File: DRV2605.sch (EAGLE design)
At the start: 107 parts, among them J1 BM06B-SRSS-TB, J2 BM06B-SRSS-TB, J3 BM06B-SRSS-TB, J4 BM06B-SRSS-TB, J5 BM06B-SRSS-TB, J6 JST_6_PIN_VERTICAL, U1 DRV2605L, U11 NRF51X22_QFQF, U2 DRV2605L, U3 DRV2605L, U4 DRV2605L, U5 DRV2605L, U6 DRV2605L, U7 BNO080, U8 TCA9548APWR, U9 TCA9548APWR, X1 32.768kHz, X2 8MHz, X4 16MHz, X5 32.768kHz, Y1 32.768kHz

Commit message: 6DRVs ARM IMU on board - done; palmIMU/battery/programming connector
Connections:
- removed net PS0/WAKE: U7.PS0/WAKE
- removed net PS1: U7.PS1
- removed net SCL/SCK/RX: R28.1, U7.H_SCL/SCLK/RX
- removed net SDA/MISO/TX: R29.1, U7.H_SDA/MISO/TX
- net EN6: now also U$9.PB14/I2S2_XD
- net GND: now also U7.PS0/WAKE, U7.PS1
- net IMU_SCL6: now also R28.1, U7.H_SCL/SCLK/RX
- net IMU_SDA6: now also R29.1, U7.H_SDA/MISO/TX
- net IN/TRIG6: now also U$9.PB15/I2S2_SD
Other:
- note added: "ARM Chip Circuit"
- note added: "BNO080"
- note added: "DRV2605"
- moved on the sheet: C1, C10, C11, C12, C2, C3, C4, C5, C6, C7, C8, C9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

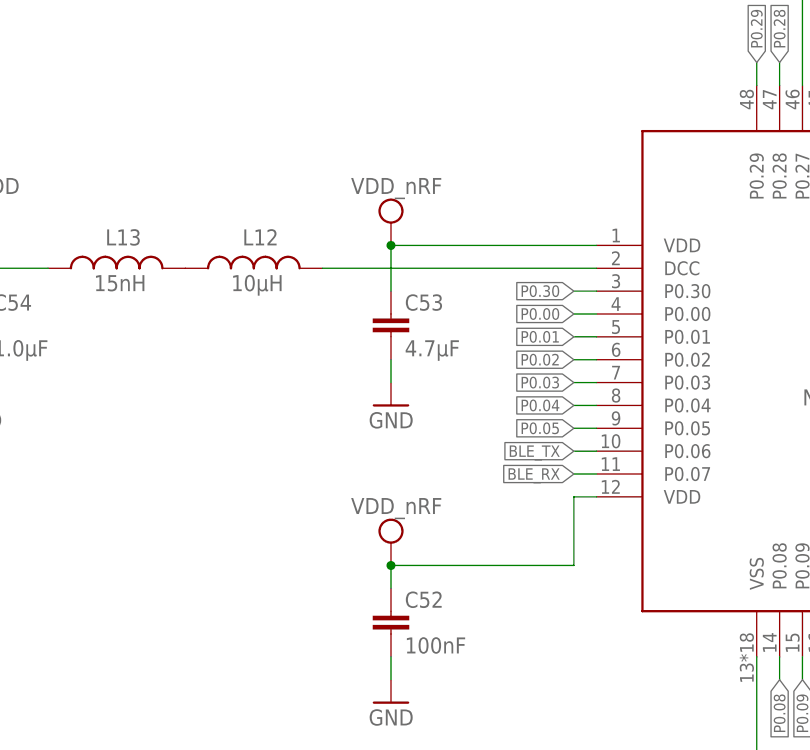
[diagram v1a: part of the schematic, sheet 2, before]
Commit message: glove connector;programming pins;NRF antenna left
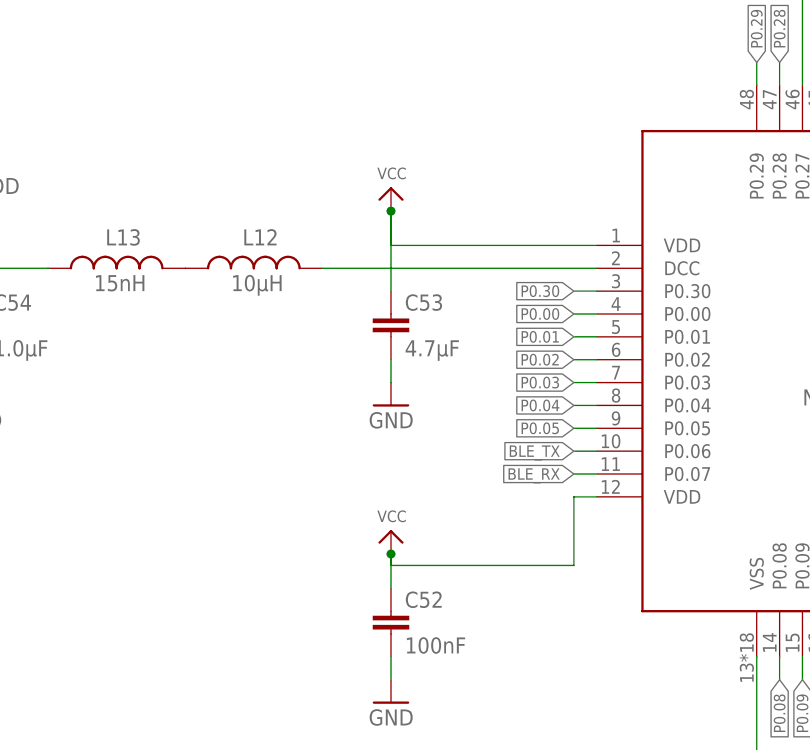
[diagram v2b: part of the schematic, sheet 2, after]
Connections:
- removed net 3.3V: C13.1, C32.1, R13.2, R14.2, R24.2, R26.2, R27.2, R28.2, R29.2, U7.VDD, U7.VDDIO
- removed net VDD_NRF: C52.1, C53.1, U11.VDD@01, U11.VDD@12
- net VCC: now also C13.1, C32.1, C52.1, C53.1, R13.2, R14.2, R24.2, R26.2, R27.2, R28.2, R29.2, U11.VDD@01, U11.VDD@12, U7.VDD, U7.VDDIO

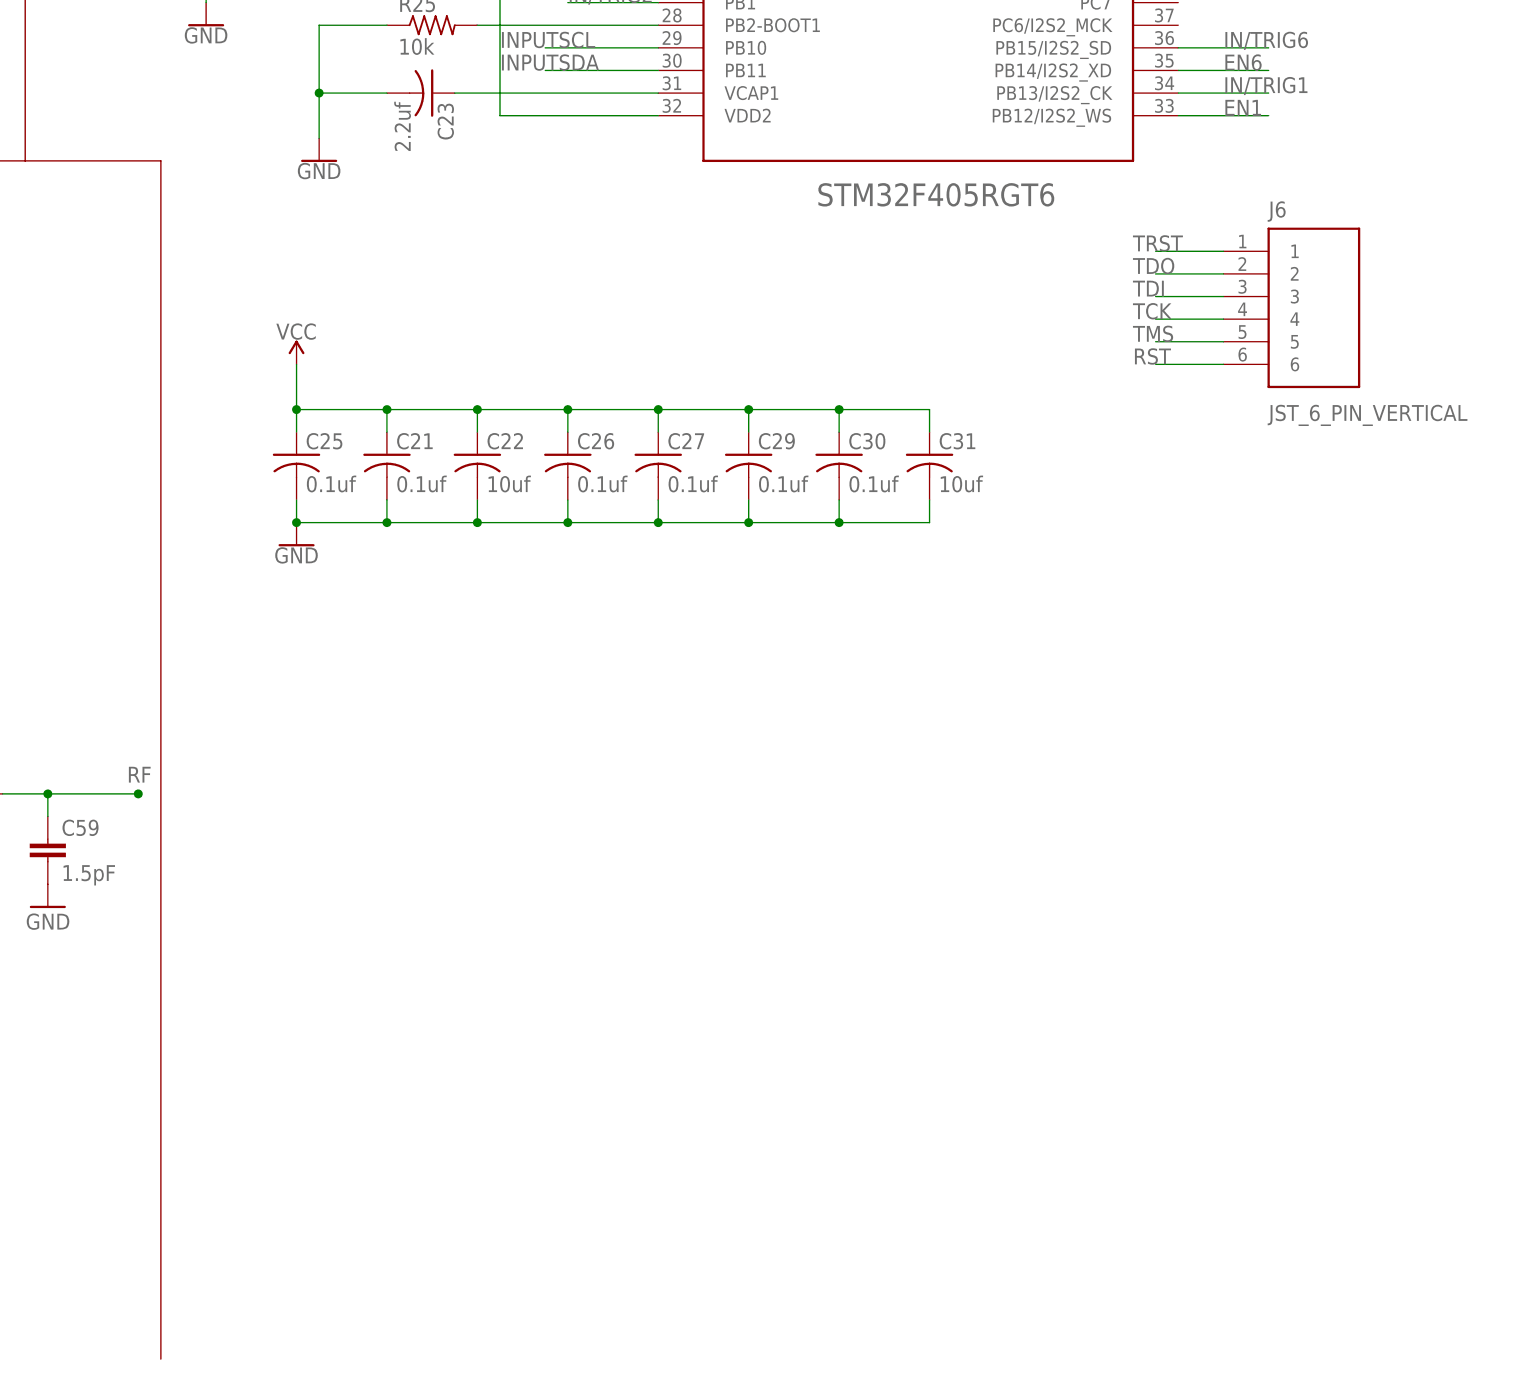
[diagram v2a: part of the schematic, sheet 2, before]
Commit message: glove connector;programming pins;NRF antenna
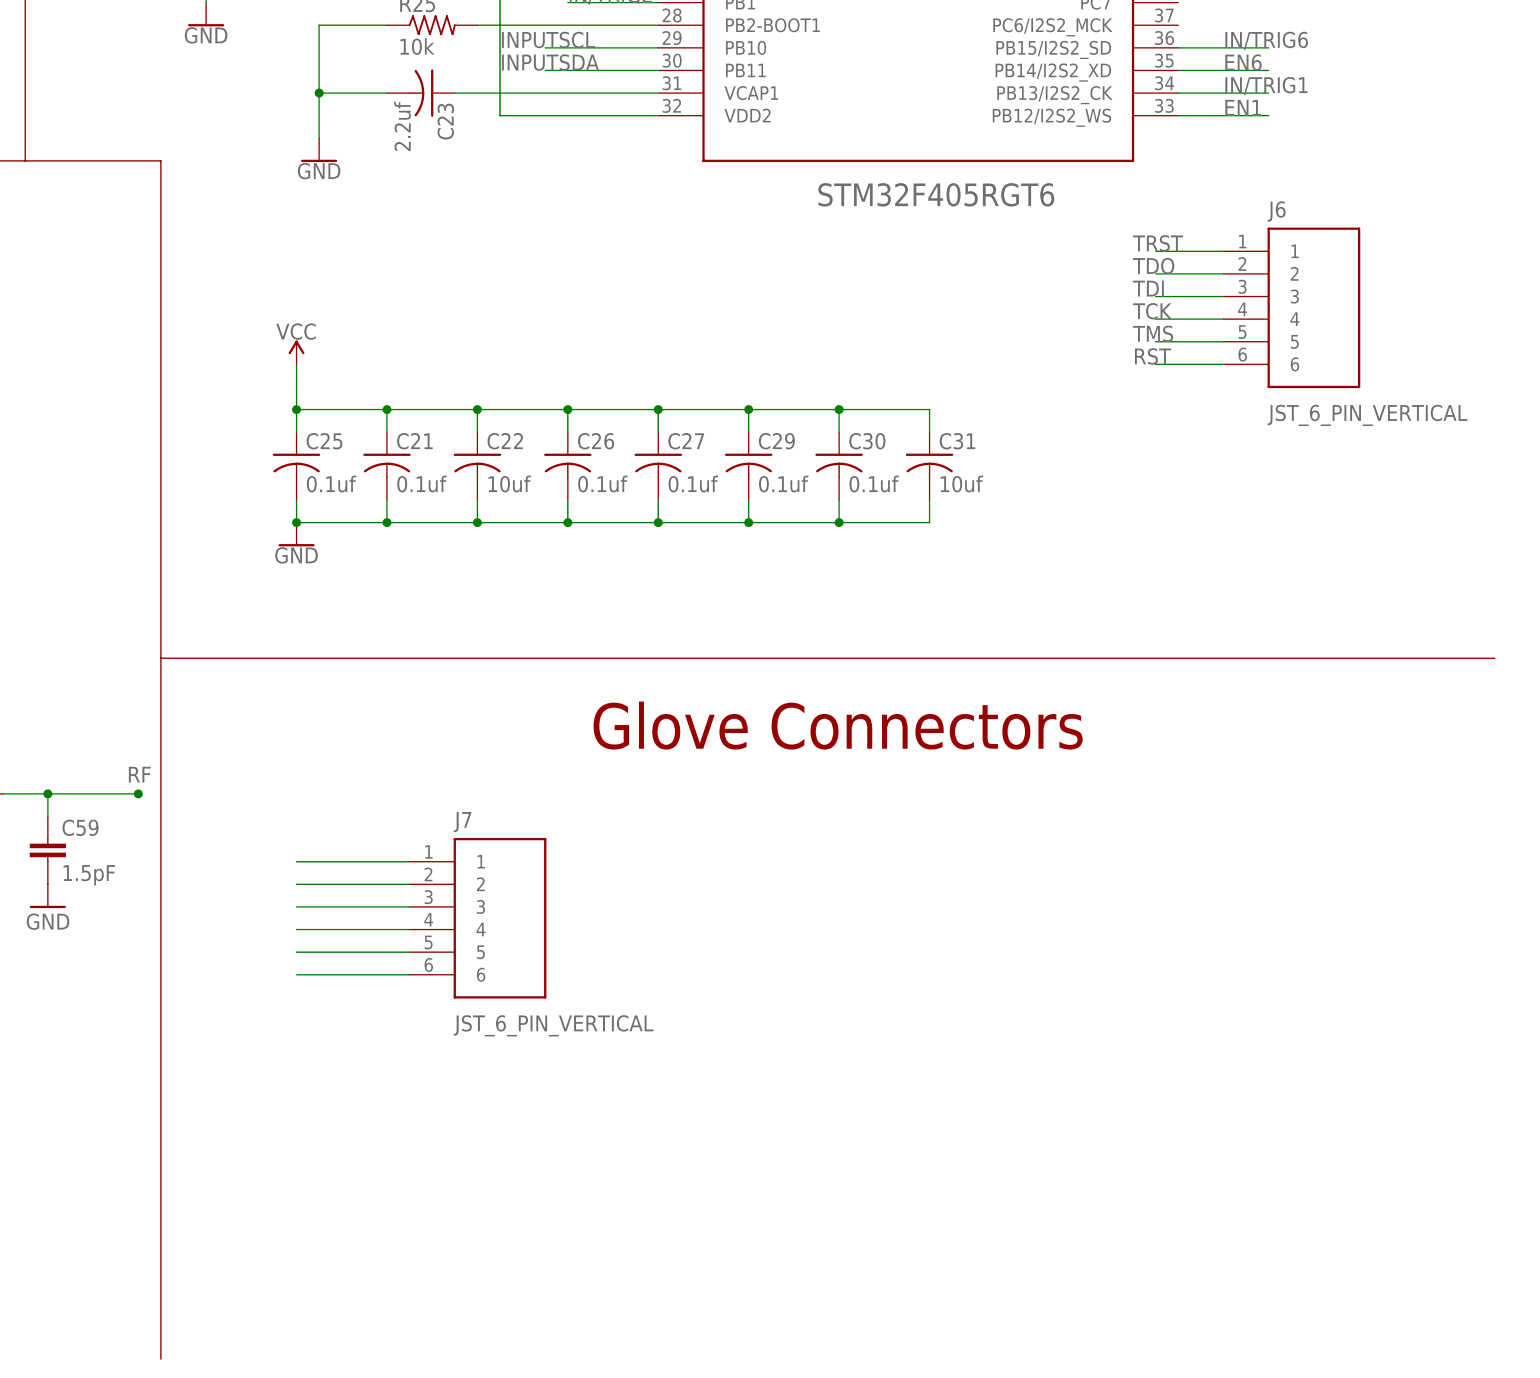
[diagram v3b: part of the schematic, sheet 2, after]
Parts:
- J7: value (none) -> JST_6_PIN_VERTICAL; device SparkFun-Connectors:CONN_04SMD2 -> SparkFun-Connectors:JST_6_PIN_VERTICAL
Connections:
- new net N$15: J7.1
- new net N$17: J7.2
- new net N$18: J7.3
- new net N$20: J7.4
- new net N$21: J7.5
- new net N$22: J7.6
- net +OUT6: no longer J7.3
- net -OUT6: no longer J7.4
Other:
- note added: "Glove Connectors"
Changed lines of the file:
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@@
 <part name="J4" library="SparkFun-Connectors" deviceset="JST_6_PIN_HORIZONTAL" device="" value="BM06B-SRSS-TB"/>
 <part name="J5" library="SparkFun-Connectors" deviceset="JST_6_PIN_HORIZONTAL" device="" value="BM06B-SRSS-TB"/>
-<part name="J7" library="SparkFun-Connectors" library_urn="urn:adsk.eagle:library:513" deviceset="CONN_04" device="SMD2" package3d_urn="urn:adsk.eagle:package:38096/1"/>
 <part name="U8" library="microbuilder" deviceset="TCA9548A" device="" value=" TCA9548APWR"/>
 <part name="R15" library="rcl" library_urn="urn:adsk.eagle:library:334" deviceset="R-US_" device="R0402" package3d_urn="urn:adsk.eagle:package:23547/2" value="10K"/>
@@
 <part name="P+11" library="microbuilder" deviceset="VCC" device=""/>
 <part name="P+12" library="microbuilder" deviceset="VCC" device=""/>
+<part name="J7" library="SparkFun-Connectors" library_urn="urn:adsk.eagle:library:513" deviceset="JST_6_PIN_VERTICAL" device="" package3d_urn="urn:adsk.eagle:package:38270/1"/>
 </parts>
 <sheets>
@@
 <instance part="J4" gate="A" x="142.24" y="30.48" rot="R180"/>
 <instance part="J5" gate="A" x="331.47" y="220.98" rot="R180"/>
-<instance part="J7" gate="G$1" x="331.47" y="157.48" rot="R180"/>
 <instance part="SUPPLY19" gate="G$1" x="317.5" y="64.77"/>
 <instance part="GND13" gate="1" x="317.5" y="49.53"/>
@@
 <label x="284.48" y="157.48" size="1.778" layer="95"/>
 </segment>
-<segment>
-<pinref part="J7" gate="G$1" pin="4"/>
-<wire x1="326.39" y1="152.4" x2="318.77" y2="152.4" width="0.1524" layer="91"/>
-<wire x1="318.77" y1="152.4" x2="317.5" y2="152.4" width="0.1524" layer="91"/>
-<label x="316.23" y="152.4" size="1.778" layer="95"/>
-</segment>
 </net>
 <net name="+OUT6" class="0">
@@
 <wire x1="279.4" y1="152.4" x2="287.02" y2="152.4" width="0.1524" layer="91"/>
 <label x="284.48" y="152.4" size="1.778" layer="95"/>
-</segment>
-<segment>
-<pinref part="J7" gate="G$1" pin="3"/>
-<wire x1="326.39" y1="154.94" x2="317.5" y2="154.94" width="0.1524" layer="91"/>
-<label x="317.5" y="154.94" size="1.778" layer="95"/>
 </segment>
 </net>
@@
 <wire x1="218.44" y1="137.16" x2="218.44" y2="256.54" width="0.1524" layer="94"/>
 <wire x1="218.44" y1="137.16" x2="233.68" y2="137.16" width="0.1524" layer="94"/>
-<wire x1="233.68" y1="137.16" x2="233.68" y2="2.54" width="0.1524" layer="94"/>
+<wire x1="233.68" y1="137.16" x2="233.68" y2="81.28" width="0.1524" layer="94"/>
 <text x="78.74" y="243.84" size="5.08" layer="94">TCA Chip Circuit</text>
+<wire x1="233.68" y1="81.28" x2="233.68" y2="2.54" width="0.1524" layer="94"/>
 <wire x1="45.72" y1="134.62" x2="45.72" y2="96.52" width="0.254" layer="97"/>
 <wire x1="45.72" y1="96.52" x2="91.44" y2="96.52" width="0.254" layer="97"/>
@@
 <text x="360.68" y="251.46" size="1.778" layer="94">Boot from flash</text>
 <text x="287.02" y="246.38" size="5.08" layer="94">ARM Chip Circuit</text>
+<wire x1="233.68" y1="81.28" x2="383.54" y2="81.28" width="0.1524" layer="94"/>
+<text x="281.94" y="71.12" size="5.08" layer="94">Glove Connectors</text>
 </plain>
 <instances>
@@
 <instance part="P+11" gate="VCC" x="55.88" y="74.93"/>
 <instance part="P+12" gate="VCC" x="55.88" y="36.83"/>
+<instance part="J7" gate="G$1" x="274.32" y="53.34"/>
 </instances>
 <busses>
@@
 </segment>
 </net>
+<net name="N$15" class="0">
+<segment>
+<pinref part="J7" gate="G$1" pin="1"/>
+<wire x1="261.62" y1="58.42" x2="248.92" y2="58.42" width="0.1524" layer="91"/>
+</segment>
+</net>
+<net name="N$17" class="0">
+<segment>
+<pinref part="J7" gate="G$1" pin="2"/>
+<wire x1="261.62" y1="55.88" x2="248.92" y2="55.88" width="0.1524" layer="91"/>
+</segment>
+</net>
+<net name="N$18" class="0">
+<segment>
+<pinref part="J7" gate="G$1" pin="3"/>
+<wire x1="261.62" y1="53.34" x2="248.92" y2="53.34" width="0.1524" layer="91"/>
+</segment>
+</net>
+<net name="N$20" class="0">
+<segment>
+<pinref part="J7" gate="G$1" pin="4"/>
+<wire x1="261.62" y1="50.8" x2="248.92" y2="50.8" width="0.1524" layer="91"/>
+</segment>
+</net>
+<net name="N$21" class="0">
+<segment>
+<pinref part="J7" gate="G$1" pin="5"/>
+<wire x1="261.62" y1="48.26" x2="248.92" y2="48.26" width="0.1524" layer="91"/>
+</segment>
+</net>
+<net name="N$22" class="0">
+<segment>
+<pinref part="J7" gate="G$1" pin="6"/>
+<wire x1="261.62" y1="45.72" x2="248.92" y2="45.72" width="0.1524" layer="91"/>
+</segment>
+</net>
